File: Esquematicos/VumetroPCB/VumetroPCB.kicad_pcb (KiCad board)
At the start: 2 copper layers, 104.1 x 144.8 mm, 16 parts, among them J1 AudioJack, U1 conn_teclado_4x4, U2 opa2350pa, U3 MAX7219, U4 MatrixLed8x8

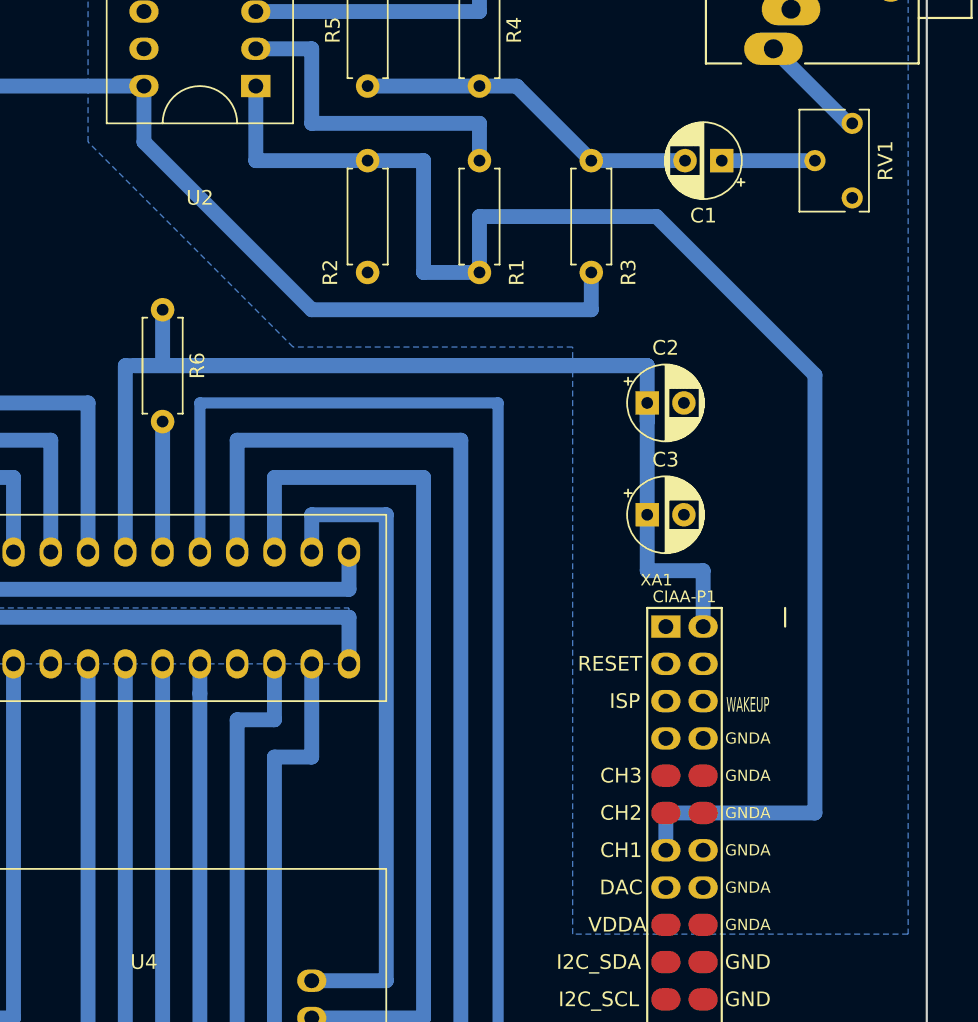
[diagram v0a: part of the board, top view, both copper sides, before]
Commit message: Cambiar la huella del potenciometro Bourns3296
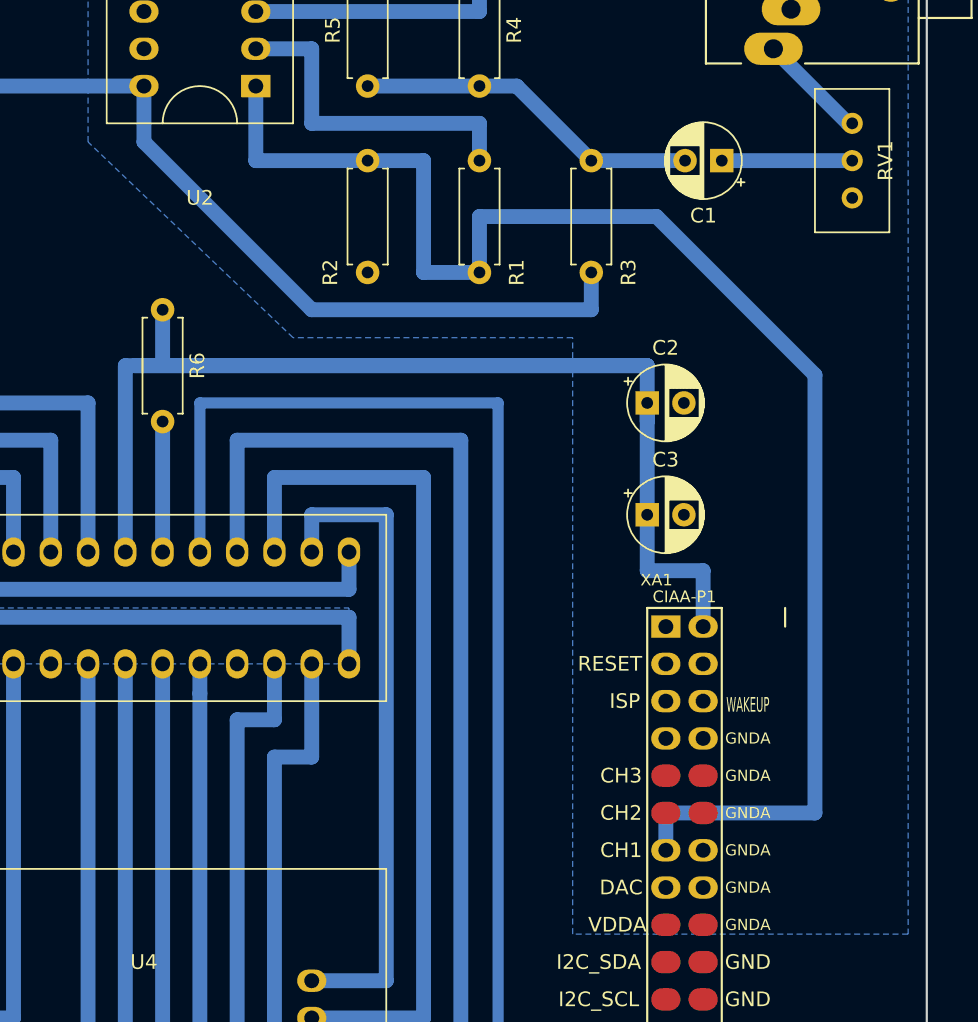
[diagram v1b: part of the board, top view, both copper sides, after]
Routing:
- net Net-(C1-Pad1): track 6.35 -> 8.89 mm
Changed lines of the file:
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@@
     (thickness 1.6)
     (drawings 10)
-    (tracks 149)
+    (tracks 148)
     (zones 0)
     (modules 16)
@@
     (33 F.Adhes user)
     (34 B.Paste user)
-    (35 F.Paste user)
+    (35 F.Paste user hide)
     (36 B.SilkS user)
     (37 F.SilkS user)
     (38 B.Mask user)
     (39 F.Mask user)
-    (40 Dwgs.User user)
+    (40 Dwgs.User user hide)
     (41 Cmts.User user)
     (42 Eco1.User user)
@@
     (solder_mask_min_width 0.25)
     (aux_axis_origin 69.215 150.114)
-    (visible_elements 7FFBFFFF)
+    (visible_elements 7FFFFFFF)
     (pcbplotparams
       (layerselection 0x00020_80000000)
@@
     (add_net "Net-(R1-Pad1)")
     (add_net "Net-(R4-Pad1)")
+  )
+  (module Projecto:Potentiometer_Bourns (layer F.Cu)
+    (at 154.94 52.07 270)
+    (descr "Potentiometer, vertical, Bourns 3296W, https://www.bourns.com/pdfs/3296.pdf")
+    (tags "Potentiometer vertical Bourns 3296W")
+    (fp_text reference RV1 (at -2.54 -2.27 270) (layer F.SilkS)
+      (effects (font (size 1 1) (thickness 0.15)))
+    )
+    (fp_text value 10K (at -2.54 4.73 270) (layer F.Fab)
+      (effects (font (size 1 1) (thickness 0.15)))
+    )
+    (fp_text user %R (at -3.175 1.23 270) (layer F.Fab)
+      (effects (font (size 0.91 0.91) (thickness 0.15)))
+    )
+    (fp_line (start 2.5 -2.7) (end -7.6 -2.7) (layer F.CrtYd) (width 0.05))
+    (fp_line (start 2.5 2.7) (end 2.5 -2.7) (layer F.CrtYd) (width 0.05))
+    (fp_line (start -7.6 2.7) (end 2.5 2.7) (layer F.CrtYd) (width 0.05))
+    (fp_line (start -7.6 -2.7) (end -7.6 2.7) (layer F.CrtYd) (width 0.05))
+    (fp_line (start 2.345 -2.53) (end 2.345 2.54) (layer F.SilkS) (width 0.12))
+    (fp_line (start -7.425 -2.53) (end -7.425 2.54) (layer F.SilkS) (width 0.12))
+    (fp_line (start -7.425 2.54) (end 2.345 2.54) (layer F.SilkS) (width 0.12))
+    (fp_line (start -7.425 -2.53) (end 2.345 -2.53) (layer F.SilkS) (width 0.12))
+    (fp_line (start 0.955 2.235) (end 0.956 0.066) (layer F.Fab) (width 0.1))
+    (fp_line (start 0.955 2.235) (end 0.956 0.066) (layer F.Fab) (width 0.1))
+    (fp_line (start 2.225 -2.41) (end -7.305 -2.41) (layer F.Fab) (width 0.1))
+    (fp_line (start 2.225 2.42) (end 2.225 -2.41) (layer F.Fab) (width 0.1))
+    (fp_line (start -7.305 2.42) (end 2.225 2.42) (layer F.Fab) (width 0.1))
+    (fp_line (start -7.305 -2.41) (end -7.305 2.42) (layer F.Fab) (width 0.1))
+    (fp_circle (center 0.955 1.15) (end 2.05 1.15) (layer F.Fab) (width 0.1))
+    (pad 3 thru_hole circle (at -5.08 0 270) (size 1.44 1.44) (drill 0.8) (layers *.Cu *.Mask)
+      (net 4 "Net-(J1-Pad2)"))
+    (pad 2 thru_hole circle (at -2.54 0 270) (size 1.44 1.44) (drill 0.8) (layers *.Cu *.Mask)
+      (net 1 "Net-(C1-Pad1)"))
+    (pad 1 thru_hole circle (at 0 0 270) (size 1.44 1.44) (drill 0.8) (layers *.Cu *.Mask)
+      (net 3 GNDA))
+    (model ${KISYS3DMOD}/Potentiometer_THT.3dshapes/Potentiometer_Bourns_3296W_Vertical.wrl
+      (at (xyz 0 0 0))
+      (scale (xyz 1 1 1))
+      (rotate (xyz 0 0 0))
+    )
   )
   (module Projecto:Conn_Poncho_Personalizado (layer F.Cu)
@@
     )
   )
-  (module Projecto:Potentiometer_Bourns (layer F.Cu)
-    (at 154.94 52.07 270)
-    (descr "Potentiometer, vertical, Bourns 3266W, https://www.bourns.com/docs/Product-Datasheets/3266.pdf")
-    (tags "Potentiometer vertical Bourns 3266W")
-    (fp_text reference RV1 (at -2.54 -2.27 270) (layer F.SilkS)
-      (effects (font (size 1 1) (thickness 0.15)))
-    )
-    (fp_text value 10K (at -2.54 4.73 270) (layer F.Fab)
-      (effects (font (size 1 1) (thickness 0.15)))
-    )
-    (fp_text user %R (at -3.175 1.23 270) (layer F.Fab)
-      (effects (font (size 0.91 0.91) (thickness 0.15)))
-    )
-    (fp_line (start 1.1 -1.3) (end -6.15 -1.3) (layer F.CrtYd) (width 0.05))
-    (fp_line (start 1.1 3.75) (end 1.1 -1.3) (layer F.CrtYd) (width 0.05))
-    (fp_line (start -6.15 3.75) (end 1.1 3.75) (layer F.CrtYd) (width 0.05))
-    (fp_line (start -6.15 -1.3) (end -6.15 3.75) (layer F.CrtYd) (width 0.05))
-    (fp_line (start 0.935 0.495) (end 0.935 3.6) (layer F.SilkS) (width 0.12))
-    (fp_line (start 0.935 -1.14) (end 0.935 -0.495) (layer F.SilkS) (width 0.12))
-    (fp_line (start -6.015 0.495) (end -6.015 3.6) (layer F.SilkS) (width 0.12))
-    (fp_line (start -6.015 -1.14) (end -6.015 -0.495) (layer F.SilkS) (width 0.12))
-    (fp_line (start -6.015 3.6) (end 0.935 3.6) (layer F.SilkS) (width 0.12))
-    (fp_line (start -6.015 -1.14) (end 0.935 -1.14) (layer F.SilkS) (width 0.12))
-    (fp_line (start -0.455 3.092) (end -0.454 1.329) (layer F.Fab) (width 0.1))
-    (fp_line (start -0.455 3.092) (end -0.454 1.329) (layer F.Fab) (width 0.1))
-    (fp_line (start 0.815 -1.02) (end -5.895 -1.02) (layer F.Fab) (width 0.1))
-    (fp_line (start 0.815 3.48) (end 0.815 -1.02) (layer F.Fab) (width 0.1))
-    (fp_line (start -5.895 3.48) (end 0.815 3.48) (layer F.Fab) (width 0.1))
-    (fp_line (start -5.895 -1.02) (end -5.895 3.48) (layer F.Fab) (width 0.1))
-    (fp_circle (center -0.455 2.21) (end 0.435 2.21) (layer F.Fab) (width 0.1))
-    (pad 3 thru_hole circle (at -5.08 0 270) (size 1.44 1.44) (drill 0.8) (layers *.Cu *.Mask)
-      (net 4 "Net-(J1-Pad2)"))
-    (pad 2 thru_hole circle (at -2.54 2.54 270) (size 1.44 1.44) (drill 0.8) (layers *.Cu *.Mask)
-      (net 1 "Net-(C1-Pad1)"))
-    (pad 1 thru_hole circle (at 0 0 270) (size 1.44 1.44) (drill 0.8) (layers *.Cu *.Mask)
-      (net 3 GNDA))
-    (model ${KISYS3DMOD}/Potentiometer_THT.3dshapes/Potentiometer_Bourns_3266W_Vertical.wrl
-      (at (xyz 0 0 0))
-      (scale (xyz 1 1 1))
-      (rotate (xyz 0 0 0))
-    )
-  )
   (gr_line (start 55.88 158.75) (end 160.02 158.75) (layer Edge.Cuts) (width 0.15))
   (gr_line (start 55.88 13.97) (end 55.88 158.75) (layer Edge.Cuts) (width 0.15))
@@
   (gr_line (start 279.4 15.875) (end 186.055 15.875) (angle 90) (layer Dwgs.User) (width 0.2))
   (gr_line (start 279.4 53.975) (end 279.4 15.875) (angle 90) (layer Dwgs.User) (width 0.2))
-  (segment (start 146.05 49.53) (end 151.765 49.53) (width 1.016) (layer B.Cu) (net 1))
-  (segment (start 151.765 49.53) (end 152.4 49.53) (width 0.762) (layer B.Cu) (net 1))
+  (segment (start 146.05 49.53) (end 154.94 49.53) (width 1.016) (layer B.Cu) (net 1))
   (segment (start 121.92 44.45) (end 129.54 44.45) (width 1.016) (layer B.Cu) (net 2))
   (segment (start 129.54 44.45) (end 132.08 44.45) (width 1.016) (layer B.Cu) (net 2))
@@
     (polygon
       (pts
-        (xy 158.75 102.235) (xy 135.89 102.235) (xy 135.89 62.23) (xy 116.84 62.23) (xy 102.87 48.26)
+        (xy 158.75 102.235) (xy 135.89 102.235) (xy 135.89 61.595) (xy 116.84 61.595) (xy 102.87 48.26)
         (xy 102.87 27.94) (xy 158.75 27.94)
       )

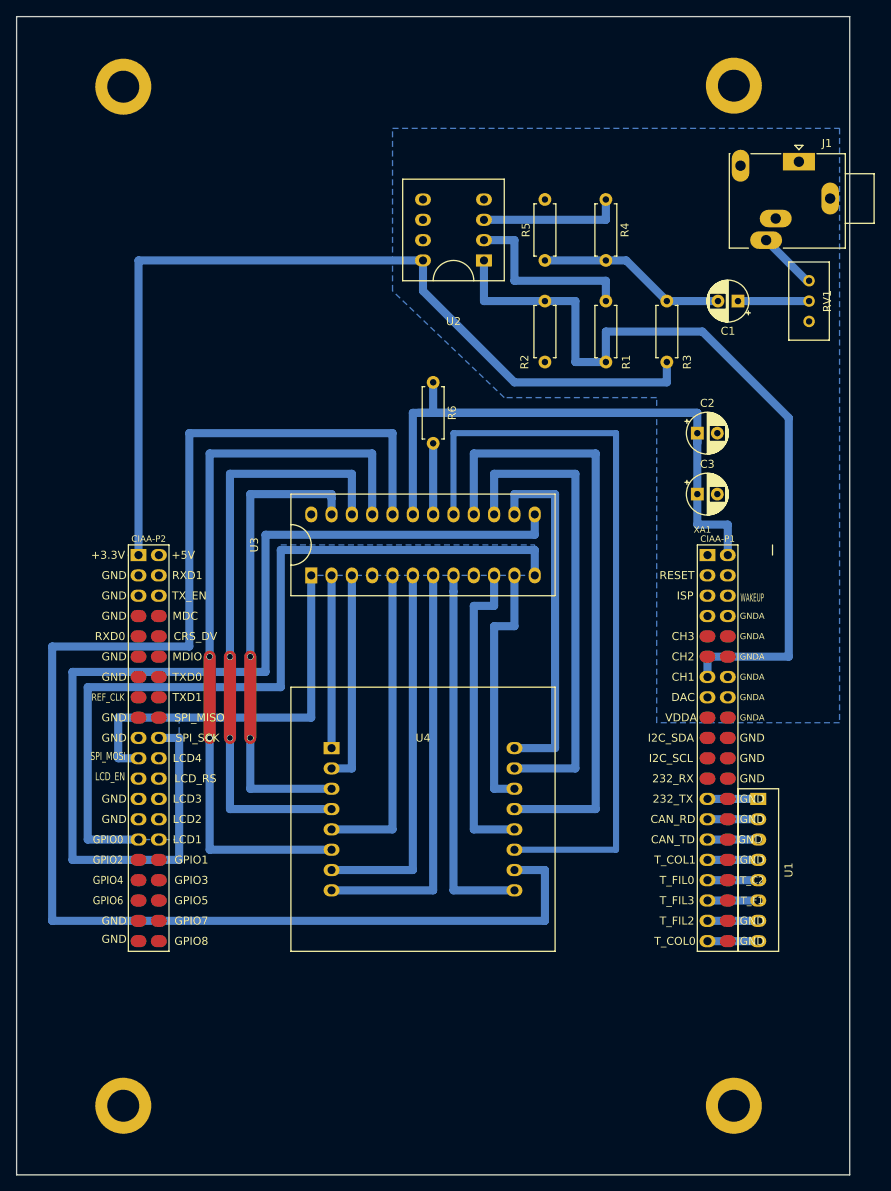
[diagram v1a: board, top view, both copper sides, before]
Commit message: Correcciones al diseño del PCB.
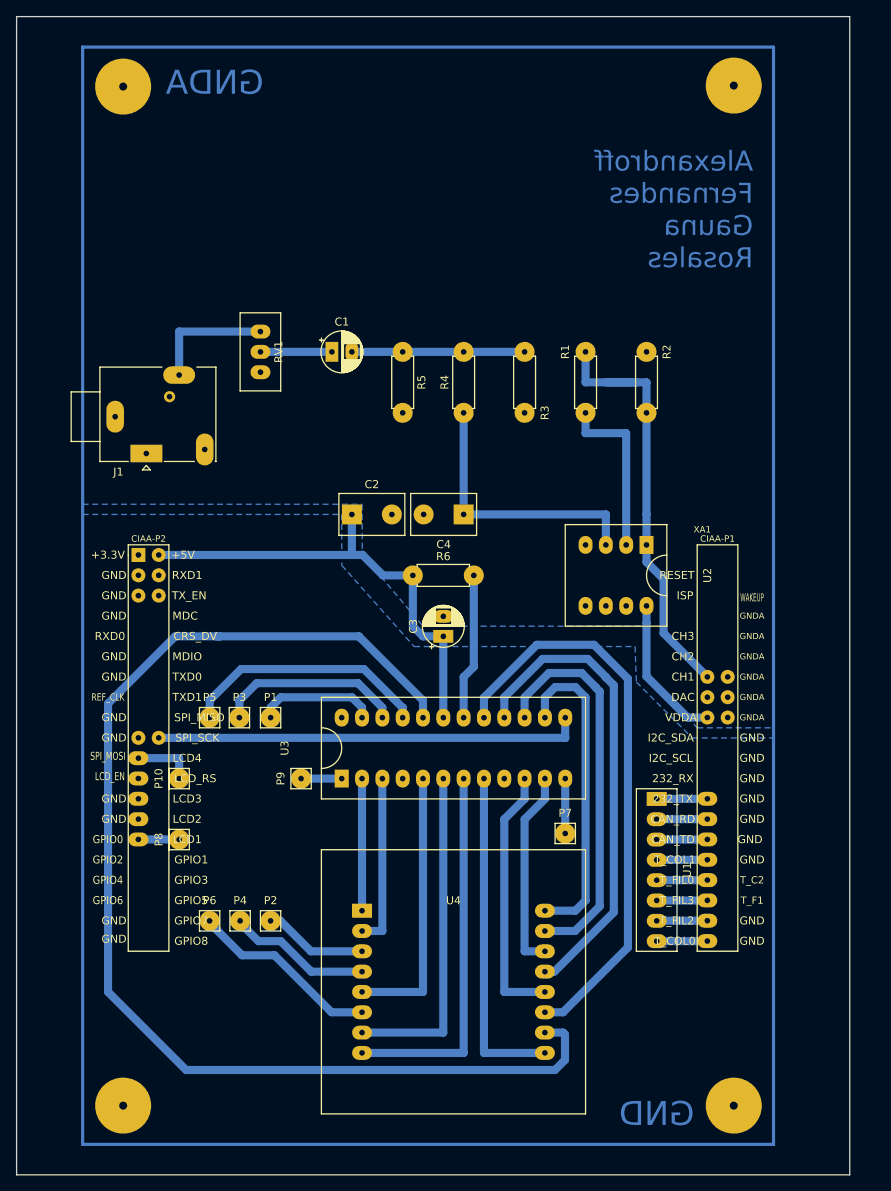
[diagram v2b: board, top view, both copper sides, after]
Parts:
- added C4: 1.8nF, Projecto:Capacitor_Disco, F.Cu at (111.8, 76.2)
- added P1: Pin_Puente, Projecto:Pin_Puente, F.Cu at (87.6, 98.6)
- added P10: Pin_Puente, Projecto:Pin_Puente, F.Cu at (73.2, 109.2)
- added P2: Pin_Puente, Projecto:Pin_Puente, F.Cu at (87.6, 124.0)
- added P3: Pin_Puente, Projecto:Pin_Puente, F.Cu at (83.7, 98.6)
- added P4: Pin_Puente, Projecto:Pin_Puente, F.Cu at (83.8, 124.0)
- added P5: Pin_Puente, Projecto:Pin_Puente, F.Cu at (80.0, 98.6)
- added P6: Pin_Puente, Projecto:Pin_Puente, F.Cu at (80.0, 124.0)
- added P7: Pin_Puente, Projecto:Pin_Puente, F.Cu at (124.5, 113.0)
- added P8: Pin_Puente, Projecto:Pin_Puente, F.Cu at (73.2, 116.8)
- added P9: Pin_Puente, Projecto:Pin_Puente, F.Cu at (88.4, 109.2)
- C2: footprint Projecto:Capacitor -> Projecto:Capacitor_Disco
- XA1: value Conn_Poncho2P_2x_20x2 -> Conn_Poncho2P_2x_20x2_personalizado
- moved J1 89.4 mm to (72.1, 68.6), turned to 0 degrees
- moved RV1 68.9 mm to (86.4, 58.4)
- moved C1 51.2 mm to (95.3, 55.9), turned to 0 degrees
- moved U2 47.7 mm to (130.8, 83.8), turned to 270 degrees
- moved C2 44.4 mm to (97.8, 76.2)
- moved C3 36.4 mm to (109.2, 91.4), turned to 90 degrees
- moved R4 32.1 mm to (111.8, 63.5), turned to 90 degrees
- moved U3 25.7 mm to (110.5, 105.4)
- moved R6 24.3 mm to (105.4, 83.8), turned to 0 degrees
- moved R5 21.1 mm to (104.1, 55.9), turned to 270 degrees
- moved U4 20.7 mm to (110.5, 134.6)
- moved R2 18.9 mm to (134.6, 63.5), turned to 90 degrees
- moved R3 18.9 mm to (119.4, 63.5)
- moved R1 14.2 mm to (127.0, 63.5), turned to 90 degrees
- moved U1 12.7 mm to (135.9, 120.7)
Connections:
- R3 pad 1: +3.3V -> (no net)
- U2 pad 8: +3.3V -> /VDDA
- U3 pad 1: /SPI_MOSI -> /SPI_MOSI(U3)
- U3 pad 12: /GPIO0 -> /GPIO0(U3)
- U3 pad 21: /COL5 -> /COL5(U3)
- U3 pad 22: /COL3 -> /COL3(U3)
- U3 pad 23: /COL2 -> /COL2(U3)
- U4 pad 3: /COL2 -> /COL2(U4)
- U4 pad 4: /COL3 -> /COL3(U4)
- U4 pad 6: /COL5 -> /COL5(U4)
- XA1 pad 16: (no net) -> GNDA
- XA1 pad 17: (no net) -> /VDDA
- XA1 pad 18: (no net) -> GNDA
- XA1 pad 41: +3.3V -> (no net)
- XA1 pad 42: (no net) -> +5V
- XA1 pad 43: (no net) -> /GND
- XA1 pad 45: (no net) -> /GND
- XA1 pad 61: /SPI_MOSI -> /SPI_MOSI(CIAA)
- XA1 pad 69: /GPIO0 -> /GPIO0(CIAA)
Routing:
- net +3.3V: track 114.0 -> 0.00 mm
- net /GPIO0: track 101.6 -> 0.00 mm
- net +5V: track 155.6 -> 58.8 mm
- net /COL5: track 92.7 -> 0.00 mm, vias 2 -> 0
- net /SPI_CLK: track 132.3 -> 53.6 mm
- net /COL3: track 74.9 -> 0.00 mm, vias 2 -> 0
- net /COL2: track 59.7 -> 0.00 mm, vias 2 -> 0
- net /SPI_MOSI: track 49.5 -> 0.00 mm
- net /CH1: track 101.6 -> 55.2 mm
- net /COL4: track 185.4 -> 152.3 mm
- net /COL5(U3): track 0.00 -> 31.2 mm
- net /COL5(U4): track 0.00 -> 23.9 mm
- net /COL3(U3): track 0.00 -> 23.4 mm
- net /COL6: track 95.2 -> 72.3 mm
- net /VDDA: track 0.00 -> 18.6 mm
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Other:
- net class Default: clearance 0.508 -> 0.75; trace_width 0.381 -> 0.8; via_dia 0.6 -> 2; via_drill 0.4 -> 0.7
- rule trace_clearance: 0.508 -> 0.75
- rule trace_min: 0.2 -> 0.8
- rule via_min_size: 0.4 -> 0.7
- board text added: "Alexandroff Fernandes Gauna Rosales"
- board text added: "GND"
- board text added: "GNDA"

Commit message: Arreglar la conexión de la resistencia R3
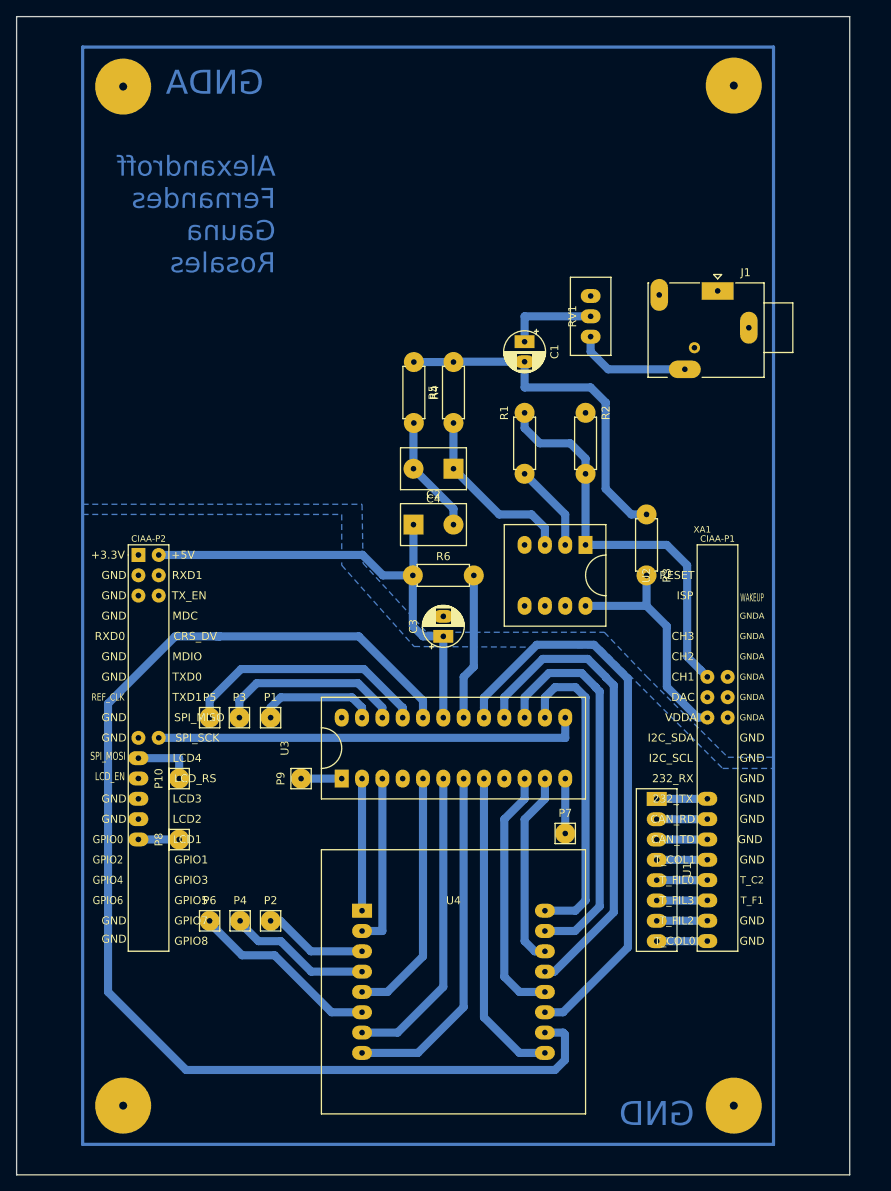
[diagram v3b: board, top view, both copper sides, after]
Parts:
- moved J1 74.2 mm to (143.5, 48.3), turned to 180 degrees
- moved RV1 42.4 mm to (127.6, 48.9), turned to 90 degrees
- moved R3 25.4 mm to (134.6, 83.8)
- moved C1 24.1 mm to (119.4, 54.6), turned to 270 degrees
- moved R1 10.8 mm to (119.4, 71.1)
- moved R2 10.8 mm to (127.0, 71.1)
- moved C2 7.80 mm to (105.5, 77.5)
- moved U2 7.62 mm to (123.2, 83.8)
- moved C4 5.85 mm to (110.5, 70.5)
- moved R5 1.89 mm to (105.5, 57.1)
- moved R4 1.80 mm to (110.5, 64.8)
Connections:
- R3 pad 1: (no net) -> /VDDA
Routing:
- net Net-(C1-Pad2): track 21.6 -> 45.2 mm
- net GNDA: track 0.00 -> 14.8 mm
- net Net-(C4-Pad1): track 34.3 -> 22.3 mm
- net /VDDA: track 18.6 -> 29.3 mm
- net Net-(R1-Pad1): track 21.6 -> 11.0 mm
- net /CH1: track 55.2 -> 50.7 mm
- net /ROW6: track 41.9 -> 38.6 mm
- net /ROW3: track 47.0 -> 43.6 mm
- net /ROW8: track 34.3 -> 31.7 mm
- net /ROW1: track 41.9 -> 39.3 mm
- net Net-(C1-Pad1): track 8.93 -> 11.4 mm
- net +5V: track 58.8 -> 60.1 mm
- net /ROW4: track 32.8 -> 31.7 mm
- net Net-(J1-Pad2): track 15.6 -> 14.6 mm
- net /ROW2: track 25.2 -> 24.4 mm
